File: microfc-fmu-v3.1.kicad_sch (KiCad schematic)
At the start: 30 parts

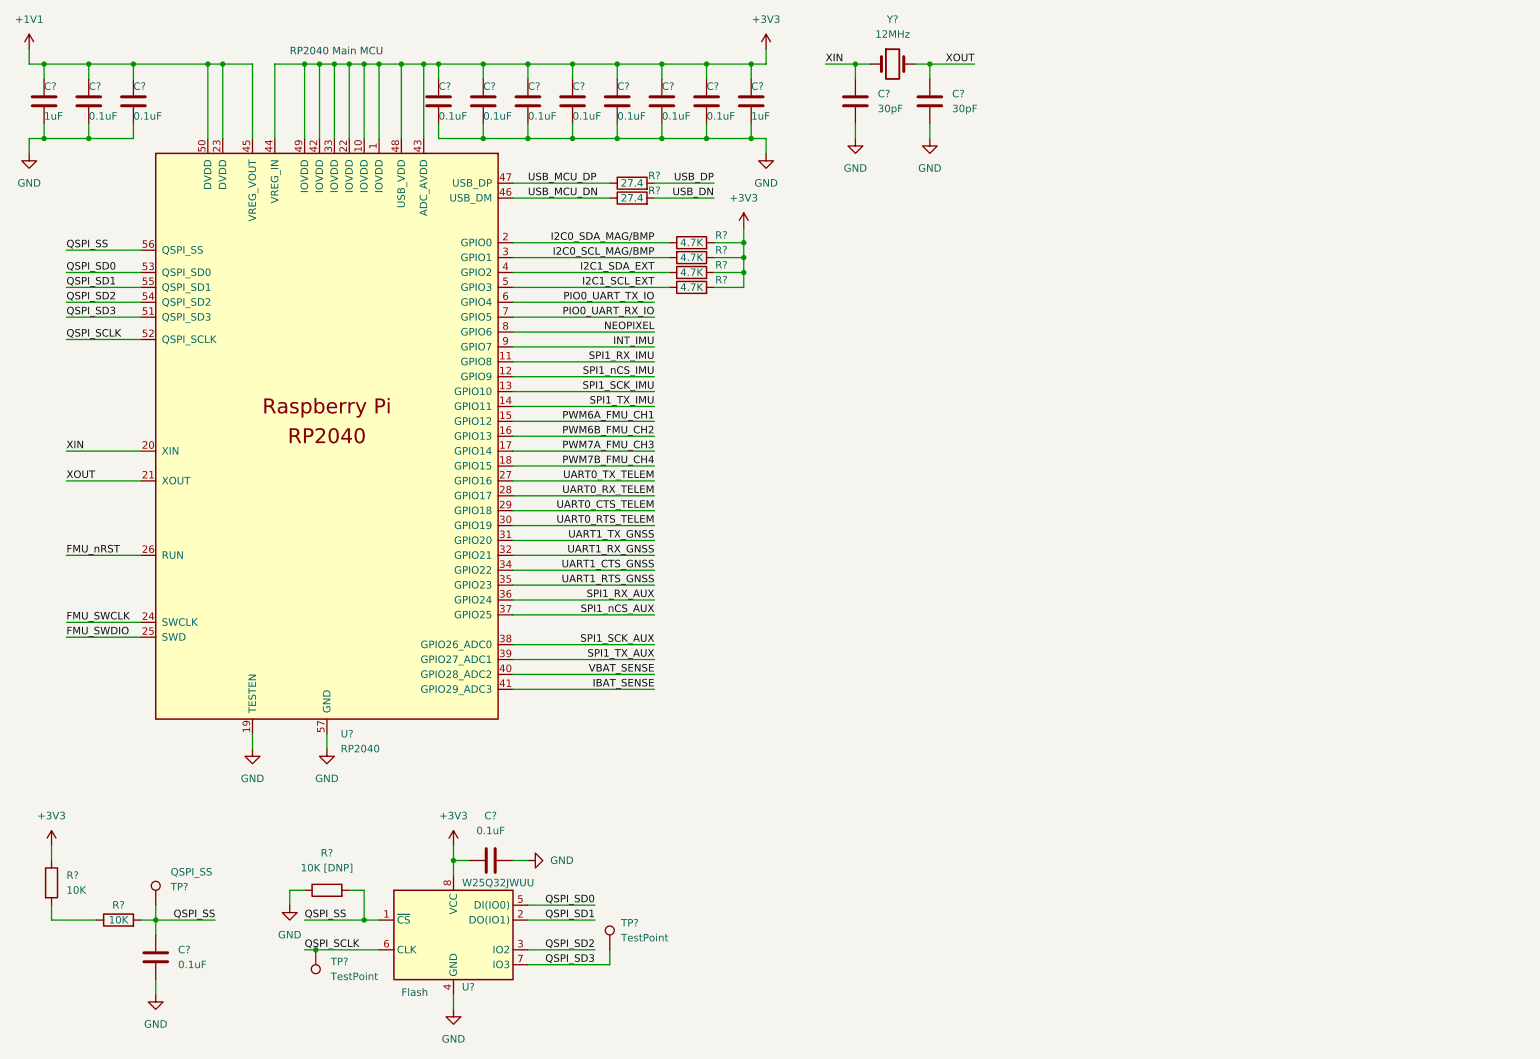
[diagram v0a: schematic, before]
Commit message: schematic: add peripherals and io
* add fmu peripherals
* add sensor suite
* add io module
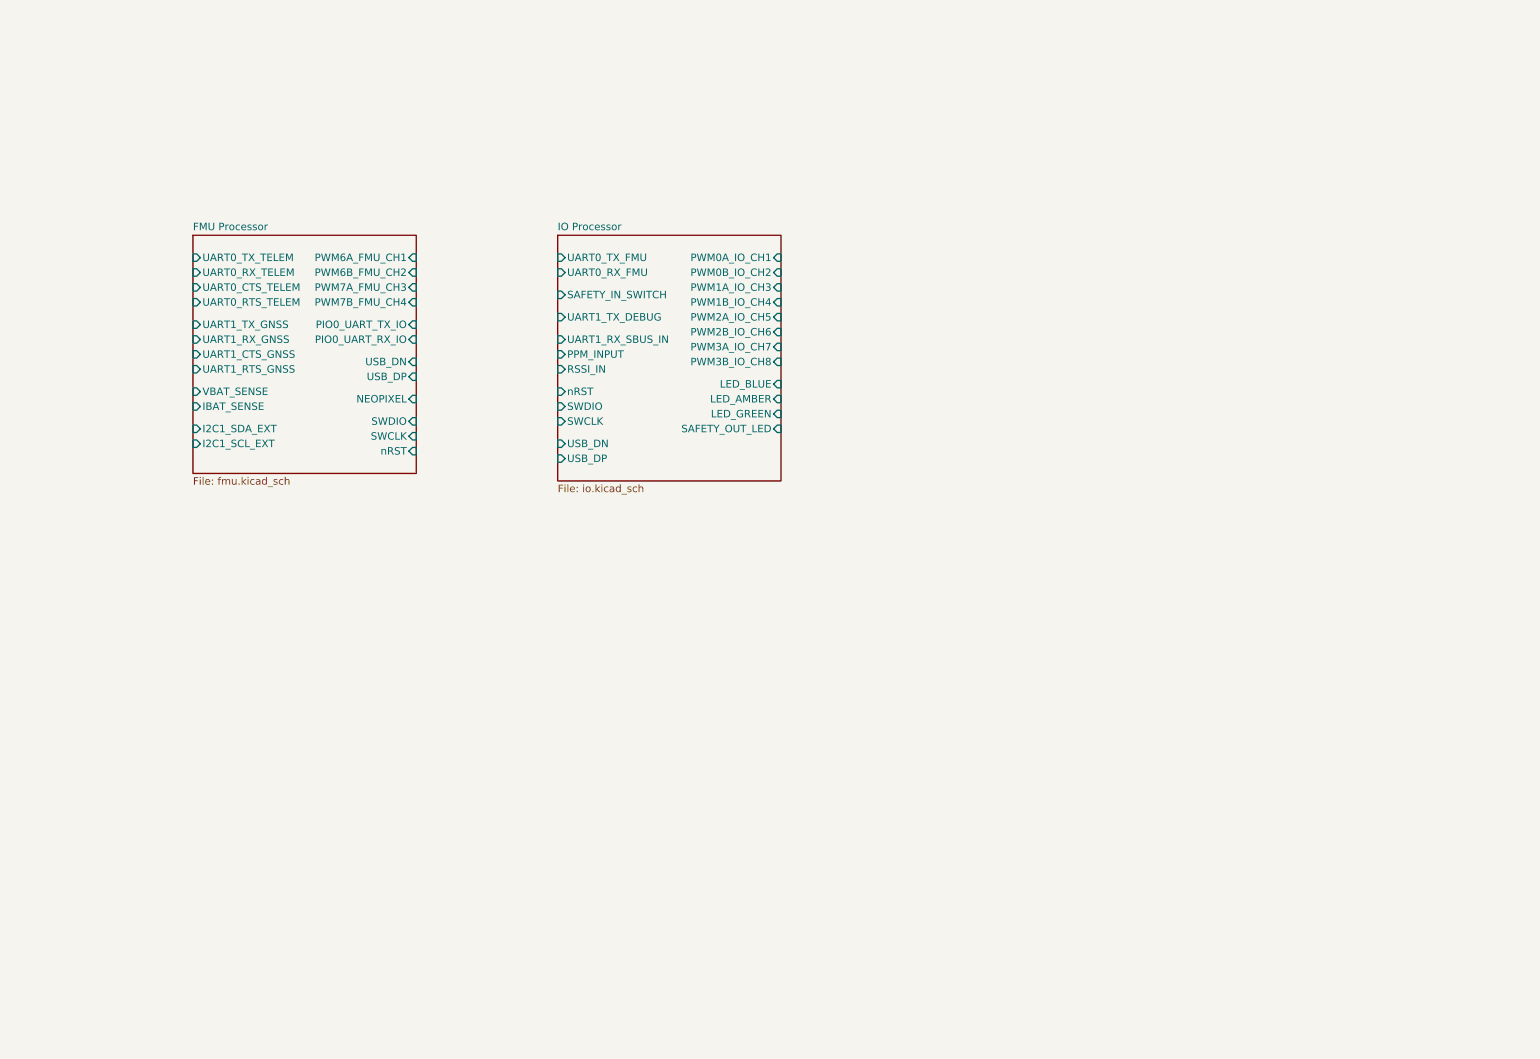
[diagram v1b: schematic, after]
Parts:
- removed C? (x11): 0.1uF, Capacitor_SMD:C_0402_1005Metric, symbol Device:C
- removed C? (x2): 30pF, Capacitor_SMD:C_0402_1005Metric, symbol Device:C
- removed C? (x2): 1uF, Capacitor_SMD:C_0402_1005Metric, symbol Device:C
- removed R? (x4): 4.7K, Resistor_SMD:R_0402_1005Metric, symbol Device:R
- removed R? (x2): 10K, Resistor_SMD:R_0402_1005Metric, symbol Device:R
- removed R?: 10K [DNP], Resistor_SMD:R_0402_1005Metric, symbol Device:R
- removed R? (x2): 27.4, Resistor_SMD:R_0402_1005Metric, symbol Device:R
- removed TP? (x2): TestPoint, TestPoint:TestPoint_Pad_D1.0mm, symbol Connector:TestPoint
- removed TP?: QSPI_SS, TestPoint:TestPoint_Pad_D1.0mm, symbol Connector:TestPoint
- removed U?: W25Q32JWUU, USON:USON8, symbol Memory_Flash:W25Q32JVSS
- removed U?: RP2040, RP2040_minimal:RP2040-QFN-56, symbol MCU_RaspberryPi_RP2040:RP2040
- removed Y?: 12MHz, Crystal:Crystal_SMD_3225-4Pin_3.2x2.5mm, symbol Device:Crystal
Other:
- added sheet FMU Processor (fmu.kicad_sch)
- added sheet IO Processor (io.kicad_sch)
- note removed: "Flash"
- note removed: "RP2040 Main MCU"

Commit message: schematic: add mezanine interfaces
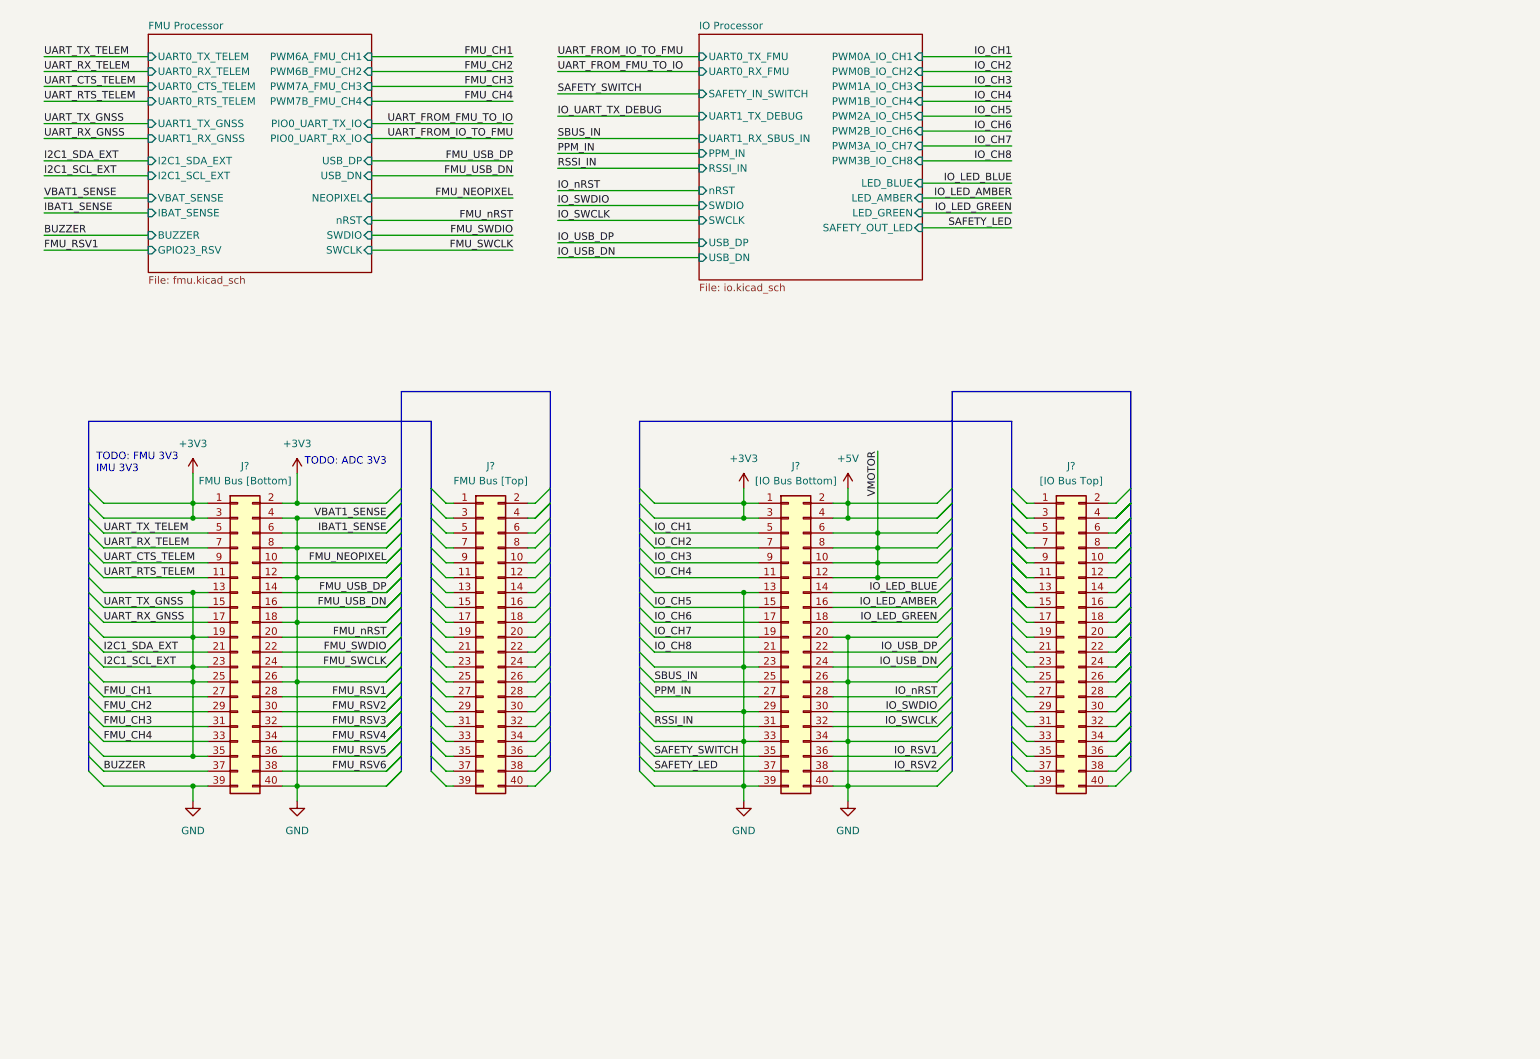
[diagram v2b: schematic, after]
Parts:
- added J?: [IO Bus Bottom], symbol Connector_Generic:Conn_02x20_Odd_Even
- added J?: [IO Bus Top], symbol Connector_Generic:Conn_02x20_Odd_Even
- added J?: FMU Bus [Bottom], symbol Connector_Generic:Conn_02x20_Odd_Even
- added J?: FMU Bus [Top], symbol Connector_Generic:Conn_02x20_Odd_Even
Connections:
- new net +3V3: J?.1 (Pin_1), J?.1 (Pin_1), J?.2 (Pin_2), J?.3 (Pin_3), J?.3 (Pin_3)
- new net +5V: J?.2 (Pin_2), J?.4 (Pin_4)
- new net BUZZER: J?.37 (Pin_37)
- new net FMU_CH1: J?.27 (Pin_27)
- new net FMU_CH2: J?.29 (Pin_29)
- new net FMU_CH3: J?.31 (Pin_31)
- new net FMU_CH4: J?.33 (Pin_33)
- new net FMU_NEOPIXEL: J?.10 (Pin_10)
- new net FMU_RSV1: J?.28 (Pin_28)
- new net FMU_RSV2: J?.30 (Pin_30)
- new net FMU_RSV3: J?.32 (Pin_32)
- new net FMU_RSV4: J?.34 (Pin_34)
- new net FMU_RSV5: J?.36 (Pin_36)
- new net FMU_RSV6: J?.38 (Pin_38)
- new net FMU_SWCLK: J?.24 (Pin_24)
- new net FMU_SWDIO: J?.22 (Pin_22)
- new net FMU_USB_DN: J?.16 (Pin_16)
- new net FMU_USB_DP: J?.14 (Pin_14)
- new net FMU_nRST: J?.20 (Pin_20)
- new net GND: J?.12 (Pin_12), J?.13 (Pin_13), J?.18 (Pin_18), J?.20 (Pin_20), J?.23 (Pin_23), J?.26 (Pin_26), J?.26 (Pin_26), J?.29 (Pin_29), J?.33 (Pin_33), J?.34 (Pin_34), J?.39 (Pin_39), J?.39 (Pin_39), J?.4 (Pin_4), J?.40 (Pin_40), J?.40 (Pin_40), J?.8 (Pin_8)
- new net I2C1_SCL_EXT: J?.13 (Pin_13), J?.19 (Pin_19), J?.23 (Pin_23), J?.25 (Pin_25), J?.35 (Pin_35)
- new net I2C1_SDA_EXT: J?.21 (Pin_21)
- new net IBAT1_SENSE: J?.6 (Pin_6)
- new net IO_CH1: J?.5 (Pin_5)
- new net IO_CH2: J?.7 (Pin_7)
- new net IO_CH3: J?.9 (Pin_9)
- new net IO_CH4: J?.11 (Pin_11)
- new net IO_CH5: J?.15 (Pin_15)
- new net IO_CH6: J?.17 (Pin_17)
- new net IO_CH7: J?.19 (Pin_19)
- new net IO_CH8: J?.21 (Pin_21)
- new net IO_LED_AMBER: J?.16 (Pin_16)
- new net IO_LED_BLUE: J?.14 (Pin_14)
- new net IO_LED_GREEN: J?.18 (Pin_18)
- new net IO_RSV1: J?.36 (Pin_36)
- new net IO_RSV2: J?.38 (Pin_38)
- new net IO_SWCLK: J?.32 (Pin_32)
- new net IO_SWDIO: J?.30 (Pin_30)
- new net IO_USB_DN: J?.24 (Pin_24)
- new net IO_USB_DP: J?.22 (Pin_22)
- new net IO_nRST: J?.28 (Pin_28)
- new net PPM_IN: J?.27 (Pin_27)
- new net RSSI_IN: J?.31 (Pin_31)
- new net SAFETY_LED: J?.37 (Pin_37)
- new net SAFETY_SWITCH: J?.35 (Pin_35)
- new net SBUS_IN: J?.25 (Pin_25)
- new net UART_CTS_TELEM: J?.9 (Pin_9)
- new net UART_RTS_TELEM: J?.11 (Pin_11)
- new net UART_RX_GNSS: J?.17 (Pin_17)
- new net UART_RX_TELEM: J?.7 (Pin_7)
- new net UART_TX_GNSS: J?.15 (Pin_15)
- new net UART_TX_TELEM: J?.5 (Pin_5)
- new net VMOTOR: J?.10 (Pin_10), J?.12 (Pin_12), J?.6 (Pin_6), J?.8 (Pin_8)
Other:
- sheet FMU Processor ports: added BUZZER, GPIO23_RSV; removed UART1_CTS_GNSS, UART1_RTS_GNSS
- sheet IO Processor ports: added PPM_IN; removed PPM_INPUT
- note added: "TODO: ADC 3V3"
- note added: "TODO: FMU 3V3 IMU 3V3"

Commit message: schematic: update power and fix errors
* specify separate 3V3 lines
* remove bus symbols due to incorrect usage
* pass ERC
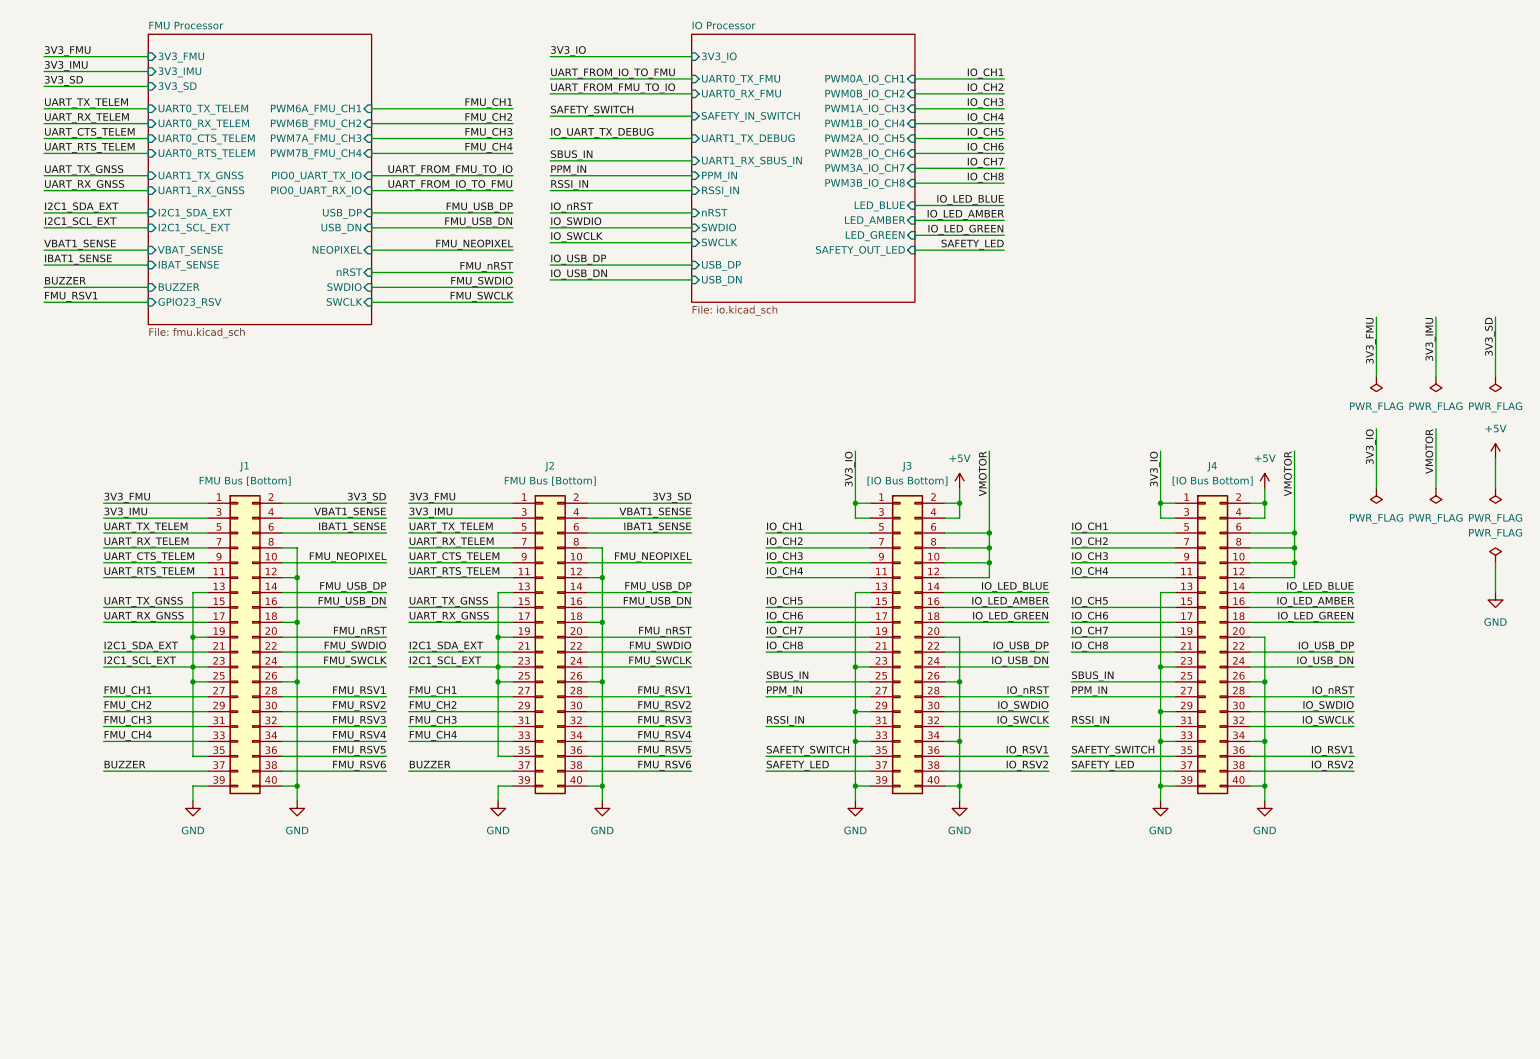
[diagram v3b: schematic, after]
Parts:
- removed J?: [IO Bus Top], symbol Connector_Generic:Conn_02x20_Odd_Even
- removed J?: FMU Bus [Top], symbol Connector_Generic:Conn_02x20_Odd_Even
- added J2: FMU Bus [Bottom], symbol Connector_Generic:Conn_02x20_Odd_Even
- added J4: [IO Bus Bottom], symbol Connector_Generic:Conn_02x20_Odd_Even
- gave numbers to parts that had none: 2
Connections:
- net +5V: now also J4.2 (Pin_2), J4.4 (Pin_4)
- net BUZZER: now also J2.37 (Pin_37)
- net FMU_CH1: now also J2.27 (Pin_27)
- net FMU_CH2: now also J2.29 (Pin_29)
- net FMU_CH3: now also J2.31 (Pin_31)
- net FMU_CH4: now also J2.33 (Pin_33)
- net FMU_NEOPIXEL: now also J2.10 (Pin_10)
- net FMU_RSV1: now also J2.28 (Pin_28)
- net FMU_RSV2: now also J2.30 (Pin_30)
- net FMU_RSV3: now also J2.32 (Pin_32)
- net FMU_RSV4: now also J2.34 (Pin_34)
- net FMU_RSV5: now also J2.36 (Pin_36)
- net FMU_RSV6: now also J2.38 (Pin_38)
- net FMU_SWCLK: now also J2.24 (Pin_24)
- net FMU_SWDIO: now also J2.22 (Pin_22)
- net FMU_USB_DN: now also J2.16 (Pin_16)
- net FMU_USB_DP: now also J2.14 (Pin_14)
- net FMU_nRST: now also J2.20 (Pin_20)
- net GND: now also J2.12 (Pin_12), J2.18 (Pin_18), J2.26 (Pin_26), J2.39 (Pin_39), J2.40 (Pin_40), J2.8 (Pin_8), J4.13 (Pin_13), J4.20 (Pin_20), J4.23 (Pin_23), J4.26 (Pin_26), J4.29 (Pin_29), J4.33 (Pin_33), J4.34 (Pin_34), J4.39 (Pin_39), J4.40 (Pin_40); no longer J1.4 (Pin_4)
- net I2C1_SCL_EXT: now also J2.13 (Pin_13), J2.19 (Pin_19), J2.23 (Pin_23), J2.25 (Pin_25), J2.35 (Pin_35)
- net I2C1_SDA_EXT: now also J2.21 (Pin_21)
- net IBAT1_SENSE: now also J2.6 (Pin_6)
- net IO_CH1: now also J4.5 (Pin_5)
- net IO_CH2: now also J4.7 (Pin_7)
- net IO_CH3: now also J4.9 (Pin_9)
- net IO_CH4: now also J4.11 (Pin_11)
- net IO_CH5: now also J4.15 (Pin_15)
- net IO_CH6: now also J4.17 (Pin_17)
- net IO_CH7: now also J4.19 (Pin_19)
- net IO_CH8: now also J4.21 (Pin_21)
- net IO_LED_AMBER: now also J4.16 (Pin_16)
- net IO_LED_BLUE: now also J4.14 (Pin_14)
- net IO_LED_GREEN: now also J4.18 (Pin_18)
- net IO_RSV1: now also J4.36 (Pin_36)
- net IO_RSV2: now also J4.38 (Pin_38)
- net IO_SWCLK: now also J4.32 (Pin_32)
- net IO_SWDIO: now also J4.30 (Pin_30)
- net IO_USB_DN: now also J4.24 (Pin_24)
- net IO_USB_DP: now also J4.22 (Pin_22)
- net IO_nRST: now also J4.28 (Pin_28)
- net PPM_IN: now also J4.27 (Pin_27)
- net RSSI_IN: now also J4.31 (Pin_31)
- net SAFETY_LED: now also J4.37 (Pin_37)
- net SAFETY_SWITCH: now also J4.35 (Pin_35)
- net SBUS_IN: now also J4.25 (Pin_25)
- net UART_CTS_TELEM: now also J2.9 (Pin_9)
- net UART_RTS_TELEM: now also J2.11 (Pin_11)
- net UART_RX_GNSS: now also J2.17 (Pin_17)
- net UART_RX_TELEM: now also J2.7 (Pin_7)
- net UART_TX_GNSS: now also J2.15 (Pin_15)
- net UART_TX_TELEM: now also J2.5 (Pin_5)
- net VMOTOR: now also J4.10 (Pin_10), J4.12 (Pin_12), J4.6 (Pin_6), J4.8 (Pin_8)
- removed net +3V3: J1.1 (Pin_1), J1.2 (Pin_2), J1.3 (Pin_3), J3.1 (Pin_1), J3.3 (Pin_3)
- new net 3V3_FMU: J1.1 (Pin_1), J2.1 (Pin_1)
- new net 3V3_IMU: J1.3 (Pin_3), J2.3 (Pin_3)
- new net 3V3_IO: J3.1 (Pin_1), J3.3 (Pin_3), J4.1 (Pin_1), J4.3 (Pin_3)
- new net 3V3_SD: J1.2 (Pin_2), J2.2 (Pin_2)
- new net VBAT1_SENSE: J1.4 (Pin_4), J2.4 (Pin_4)
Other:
- sheet FMU Processor ports: added 3V3_FMU, 3V3_IMU, 3V3_SD; removed none
- sheet IO Processor ports: added 3V3_IO; removed none
- note removed: "TODO: ADC 3V3"
- note removed: "TODO: FMU 3V3 IMU 3V3"
- moved on the sheet: J3

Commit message: schematic: fix mezanine typo
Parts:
- J2: value FMU Bus [Bottom] -> FMU Bus [Top]
- J4: value [IO Bus Bottom] -> [IO Bus Top]
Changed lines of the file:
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@@
     (in_bom yes) (on_board yes) (fields_autoplaced)
     (property "Reference" "J4" (id 0) (at 218.44 93.98 0))
-    (property "Value" "[IO Bus Bottom]" (id 1) (at 218.44 96.52 0))
+    (property "Value" "[IO Bus Top]" (id 1) (at 218.44 96.52 0))
     (property "Footprint" "" (id 2) (at 217.17 123.19 0)
       (effects (font (size 1.27 1.27)) hide)
@@
     (in_bom yes) (on_board yes) (fields_autoplaced)
     (property "Reference" "J2" (id 0) (at 105.41 93.98 0))
-    (property "Value" "FMU Bus [Bottom]" (id 1) (at 105.41 96.52 0))
+    (property "Value" "FMU Bus [Top]" (id 1) (at 105.41 96.52 0))
     (property "Footprint" "" (id 2) (at 104.14 123.19 0)
       (effects (font (size 1.27 1.27)) hide)
@@
     )
     (path "/f9937900-c7e9-484c-8c19-08a1486cee80"
-      (reference "J2") (unit 1) (value "FMU Bus [Bottom]") (footprint "")
+      (reference "J2") (unit 1) (value "FMU Bus [Top]") (footprint "")
     )
     (path "/5ae7b426-6c30-416b-966f-159e60bf5e37"
@@
     )
     (path "/a1782542-3abe-4344-b418-7870c468beab"
-      (reference "J4") (unit 1) (value "[IO Bus Bottom]") (footprint "")
+      (reference "J4") (unit 1) (value "[IO Bus Top]") (footprint "")
     )
     (path "/b7f4c42a-ec09-47f5-88b3-96098e35479a/aca8d602-9482-4cef-8c60-7c037cad9604"
